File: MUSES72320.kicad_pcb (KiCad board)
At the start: 2 copper layers, 53.2 x 33.2 mm, 30 parts, among them U1 MUSES72320V-TE2, U2 MUSES02

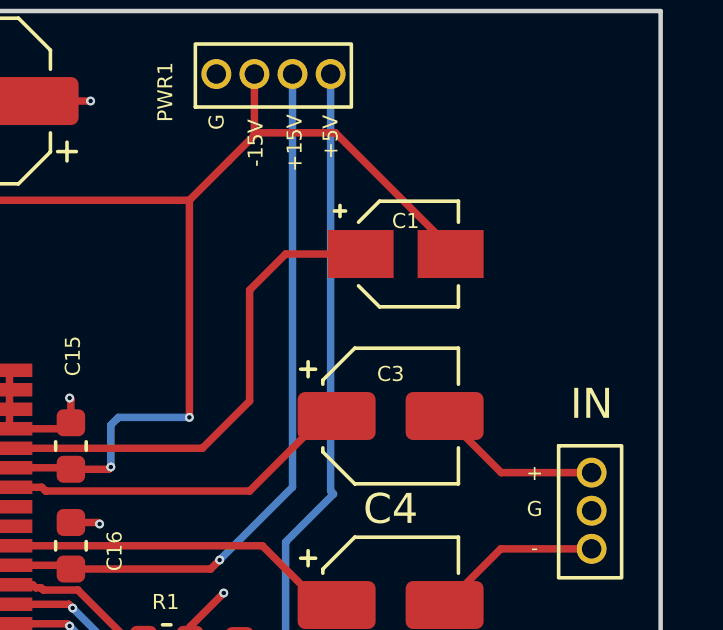
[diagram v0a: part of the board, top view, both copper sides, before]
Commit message: MUSES72320-PCB Update
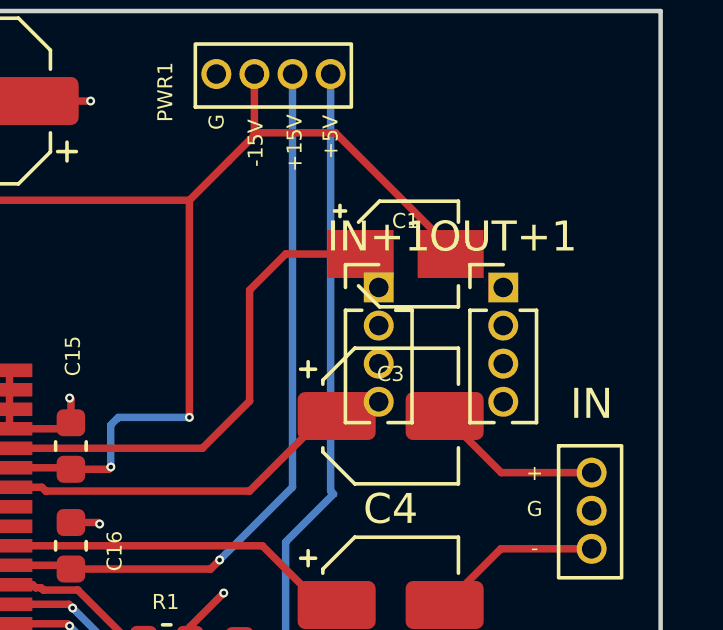
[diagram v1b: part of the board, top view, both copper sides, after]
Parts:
- added IN+1: Conn_01x04_Male, Connector_PinHeader_1.27mm:PinHeader_1x04_P1.27mm_Vertical, F.Cu at (159.0, 92.6)
- added OUT+1: Conn_01x04_Male, Connector_PinHeader_1.27mm:PinHeader_1x04_P1.27mm_Vertical, F.Cu at (163.2, 92.6)
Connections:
- C3 pad 2: Net-(IN+1-Pad1) -> Net-(C3-Pad2)
- OUT pad 2: unconnected-(OUT+1-Pad2) -> GNDPWR
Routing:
- net Net-(IN+1-Pad1): track 5.68 -> 0.00 mm
- net Net-(C3-Pad2): track 0.00 -> 5.68 mm
